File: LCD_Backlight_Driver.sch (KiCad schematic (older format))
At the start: 6 parts, among them U1 TPS61169DCKR

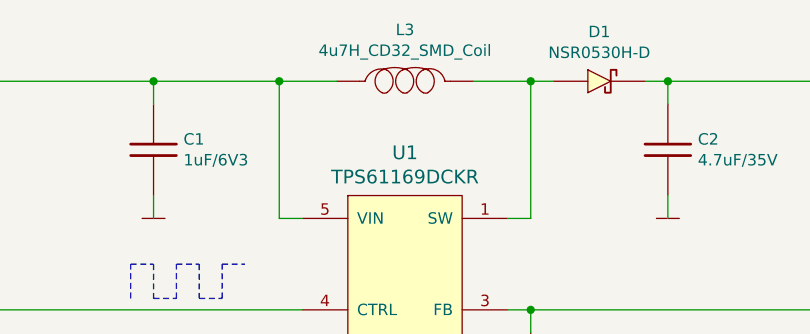
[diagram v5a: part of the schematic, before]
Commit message: Added missing URLs in BOM
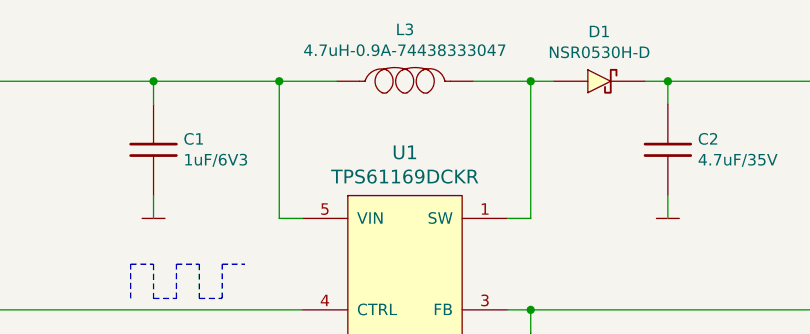
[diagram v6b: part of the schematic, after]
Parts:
- removed L3: 4u7H_CD32_SMD_Coil, Inductors:4u7H_SMD_CD32, symbol Inductors:4u7H_CD32_SMD_Coil
- added L3: 4.7uH-0.9A-74438333047, Inductors:4.7uH-0.9A-74438333047, symbol Inductors:4.7uH-0.9A-74438333047
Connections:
- net POWER_SUPPLY_2.7-5.5V: now also L3.1
- net at D1.2 (A), U1.1 (SW): now also L3.2
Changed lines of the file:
@@
 Wire Wire Line
 	5550 4300 5650 4300
-$Comp
-L Inductors:4u7H_CD32_SMD_Coil L3
-U 1 1 5E8C19B3
-P 8350 4150
-F 0 "L3" V 8575 4150 50  0000 C CNN
-F 1 "4u7H_CD32_SMD_Coil" V 8484 4150 50  0000 C CNN
-F 2 "Inductors:4u7H_SMD_CD32" H 8350 4150 50  0001 C CNN
-F 3 "Inductors/Components_Documentation/CD32.pdf" H 8350 4150 50  0001 C CNN
-	1    8350 4150
-	0    -1   -1   0
-$EndComp
 Wire Wire Line
 	8900 4150 8650 4150
@@
 Wire Wire Line
 	7250 4650 7250 4750
+$Comp
+L Inductors:4.7uH-0.9A-74438333047 L3
+U 1 1 6009C643
+P 8350 4150
+F 0 "L3" V 8575 4150 50  0000 C CNN
+F 1 "4.7uH-0.9A-74438333047" V 8484 4150 50  0000 C CNN
+F 2 "Inductors:4.7uH-0.9A-74438333047" H 8050 4150 60  0001 C CNN
+F 3 "https://pl.mouser.com/datasheet/2/445/744030004-1720746.pdf" H 8050 4150 60  0001 C CNN
+F 4 "Wurth" H 8350 4150 50  0001 C CNN "Manufacturer"
+F 5 "74438333047" H 8350 4150 50  0001 C CNN "Manufacturer Part Number"
+F 6 "Mouser" H 8350 4150 50  0001 C CNN "Supplier"
+F 7 "710-74438333047" H 8350 4150 50  0001 C CNN "Supplier Part Number"
+F 8 "https://pl.mouser.com/ProductDetail/Wurth-Elektronik/744030004?qs=2kOmHSv6VfR%252BWe9vXKDhWA%3D%3D" H 8350 4150 50  0001 C CNN "URL"
+F 9 "6,29" H 8350 4150 50  0001 C CNN "Price@1pc"
+F 10 "4,03" H 8350 4150 50  0001 C CNN "Price@1000pcs"
+F 11 "MW" H 8350 4150 50  0001 C CNN "Developer"
+F 12 "3mm x 3mm x 1mm" H 8350 4150 50  0001 C CNN "Package"
+	1    8350 4150
+	0    -1   -1   0
+$EndComp
 $EndSCHEMATC
